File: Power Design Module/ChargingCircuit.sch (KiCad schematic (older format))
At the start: 19 parts

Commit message: Charging circuit and rough layout
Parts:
- removed C?: C_Small, symbol Device:C_Small
- added JP?: Charging Current, symbol Jumper:Jumper_3_Open
- added R?: 2K, symbol Device:R_Small_US
- added R?: 8900 R, symbol Device:R_Small_US
- D?: value LED_Small_ALT -> Green; Manfacturing # (none) -> 599-0181-007F
- D?: value LED_Small_ALT -> Red; Manfacturing # (none) -> 599-0110-007F
- JP?: value SolderJumper_2_Open -> TMR OFF
- R?: value R_Small_US -> 2K
- R?: value R_Small_US -> 200k
- R?: value R_Small_US -> 1780 R
- R?: value R_Small_US -> 49.9k
- R? (x2): value R_Small_US -> 10k
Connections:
- net EN1: now also U?.6 (EN1)
- net EN2: now also U?.5 (EN2)
- net GND: now also R?.2, U?.15 (TD), R?.2, R?.2
- net at U?.12 (ILIM): now also R?.1
- net at U?.14 (TMR): now also JP?.1 (A)
- net at U?.16 (ISET): now also JP?.2 (C); no longer R?.1
- net BATT+: now reaches J?.1 (Pin_1), JP?.1 (A), U?.2 (BAT), U?.3 (BAT)
- net ~CE: now reaches U?.4 (~CE)
- net ~CE: now also R?.1
- new net: JP?.3 (B), R?.1
- new net: JP?.1 (A), R?.1
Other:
- note added: "3 + 2 -> 100mA\n1 + 2 -> 500mA"
- note added: "Jumper Configurations"
- note added: "NOTE:\ni_lim is the maximum input current set by the following ratio:\ni_lim = k_ilim / R_ilim.\nWhere k_ilim approx 1600. \nThis design i_lim is set to 800mA see 9.4 in datasheet for details."
- moved on the sheet: D?, JP?, R?

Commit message: Changes to .gitignore file
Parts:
- added D?: Green, LED_SMD:LED_0805_2012Metric_Pad1.15x1.40mm_HandSolder, symbol Device:LED_Small_ALT
- added R?: R_Small_US, symbol Device:R_Small_US
- added SW?: Charge Disable Switch, symbol Switch:SW_DIP_x01
- D? (x2): footprint (none) -> LED_SMD:LED_0805_2012Metric_Pad1.15x1.40mm_HandSolder
- J?: footprint (none) -> Connector_USB:USB_Micro-B_Molex-105017-0001
- J?: value Conn_01x02 -> Battery Output
- JP? (x2): footprint (none) -> Connector_PinHeader_2.54mm:PinHeader_1x03_P2.54mm_Vertical
- JP?: footprint (none) -> Jumper:SolderJumper-2_P1.3mm_Open_RoundedPad1.0x1.5mm
- R?: value 1780 R -> 1.78k; footprint (none) -> Resistor_SMD:R_0805_2012Metric_Pad1.15x1.40mm_HandSolder; Manfacturing # (none) -> RC0805FR-101K78L
- R?: value 2K -> 5k
- R?: value 8900 R -> 8.98k; footprint (none) -> Resistor_SMD:R_0805_2012Metric_Pad1.15x1.40mm_HandSolder; Manfacturing # (none) -> PFC-W0805LF-03-8981-B
- R? (x2): footprint (none) -> Resistor_SMD:R_0603_1608Metric_Pad1.05x0.95mm_HandSolder
- SW?: value SW_DIP_x02 -> Input Current Selection
- U?: footprint RGT16_1P7X1P7 -> BQ24072TRGTR:BQ24072TRGTR
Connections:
- net GND: now also R?.2
- net Vbus: now also SW?.2
- net Vout: now also D?.2 (A)
- net ~CE: now also SW?.1
- new net: D?.1 (K), R?.1
- no-connect marks 1 -> 3
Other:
- note added: "- All jumpers need a 0.1" (2.54mm) jumper."
- note added: "0 0 100mA\n0 1 500mA\n1 0 Ilim\n1 1 USB Standby"
- note added: "3 + 2 -> 500mA\n1 + 2 -> 100mA"
- note added: "Battery CC charger Jumper Configurations"
- note added: "Input Current Limit"
- note added: "NOTES:\n- i_lim is the maximum input current set by the following ratio:\ni_lim = k_ilim / R_ilim.\nWhere k_ilim approx 1600. \nMaking the resistance R = 2k\nThis design i_lim is set to 800mA see 9.4 in datasheet for details."
- note added: "Switch is normaly open.\nTurn to ON to Disable Charge"
- note removed: "0 0 100mA\n0 1 500mA\n1 0 Iset\n1 1 USB Standby"
- note removed: "3 + 2 -> 100mA\n1 + 2 -> 500mA"
- note removed: "Jumper Configurations"
- note removed: "NOTE:\ni_lim is the maximum input current set by the following ratio:\ni_lim = k_ilim / R_ilim.\nWhere k_ilim approx 1600. \nThis design i_lim is set to 800mA see 9.4 in datasheet for details."
- moved on the sheet: J?, R?, SW?

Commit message: Finalized Charge board
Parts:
- removed JP?: Charging Current, Connector_PinHeader_2.54mm:PinHeader_1x03_P2.54mm_Vertical, symbol Jumper:Jumper_3_Open
- removed R?: 5k, symbol Device:R_Small_US
- removed R?: 8.98k, Resistor_SMD:R_0805_2012Metric_Pad1.15x1.40mm_HandSolder, symbol Device:R_Small_US
- added C?: 4.7uF, Capacitor_SMD:C_0805_2012Metric_Pad1.15x1.40mm_HandSolder, symbol Device:C_Small
- added R?: 2K, Resistor_SMD:R_0603_1608Metric_Pad1.05x0.95mm_HandSolder, symbol Device:R_Small_US
- C?: value C_Small -> 4.7uF; footprint (none) -> Capacitor_SMD:C_0805_2012Metric_Pad1.15x1.40mm_HandSolder; Manfacturing # (none) -> C0805C475K4RAC7210
- C?: value C_Small -> 1uF; footprint (none) -> Capacitor_SMD:C_0805_2012Metric_Pad1.15x1.40mm_HandSolder; Manfacturing # (none) -> C0805C105K4RAC7210
- D? (x2): footprint LED_SMD:LED_0805_2012Metric_Pad1.15x1.40mm_HandSolder -> LED_SMD:LED_0603_1608Metric_Pad1.05x0.95mm_HandSolder; Manfacturing # 599-0181-007F -> SMLD12EN1WT86
- D?: footprint LED_SMD:LED_0805_2012Metric_Pad1.15x1.40mm_HandSolder -> LED_SMD:LED_0603_1608Metric_Pad1.05x0.95mm_HandSolder
- J?: footprint (none) -> Connector_JST:JST_PH_S2B-PH-K_1x02_P2.00mm_Horizontal; Manfacturing # (none) -> S2B-PH-K-S(LF)(SN)
- R?: footprint (none) -> Resistor_SMD:R_0603_1608Metric_Pad1.05x0.95mm_HandSolder; Manfacturing # (none) -> RN73R1JTTD2001B25
- R?: footprint (none) -> Resistor_SMD:R_0603_1608Metric_Pad1.05x0.95mm_HandSolder; Manfacturing # (none) -> RN73R1JTTD2003B25
- R?: footprint (none) -> Resistor_SMD:R_0603_1608Metric_Pad1.05x0.95mm_HandSolder; Manfacturing # (none) -> CRCW060349K9FKEAC
- R?: value R_Small_US -> 530R; footprint (none) -> Resistor_SMD:R_0603_1608Metric_Pad1.05x0.95mm_HandSolder; Manfacturing # (none) -> RN731JTTD5300F100
- R? (x2): value R_Small_US -> 320R; footprint (none) -> Resistor_SMD:R_0603_1608Metric_Pad1.05x0.95mm_HandSolder; Manfacturing # (none) -> RT0603DRE07320RL
- R? (x2): Manfacturing # (none) -> SG73G1JTTD1002D
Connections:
- net BATT+: now also C?.1
- net GND: now also R?.1, C?.2, R?.2; no longer R?.2
- net ~CE: now also R?.1
- net at U?.16 (ISET): now also R?.1
- net at D?.1 (K): now also R?.2; no longer R?.1
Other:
- moved on the sheet: R?

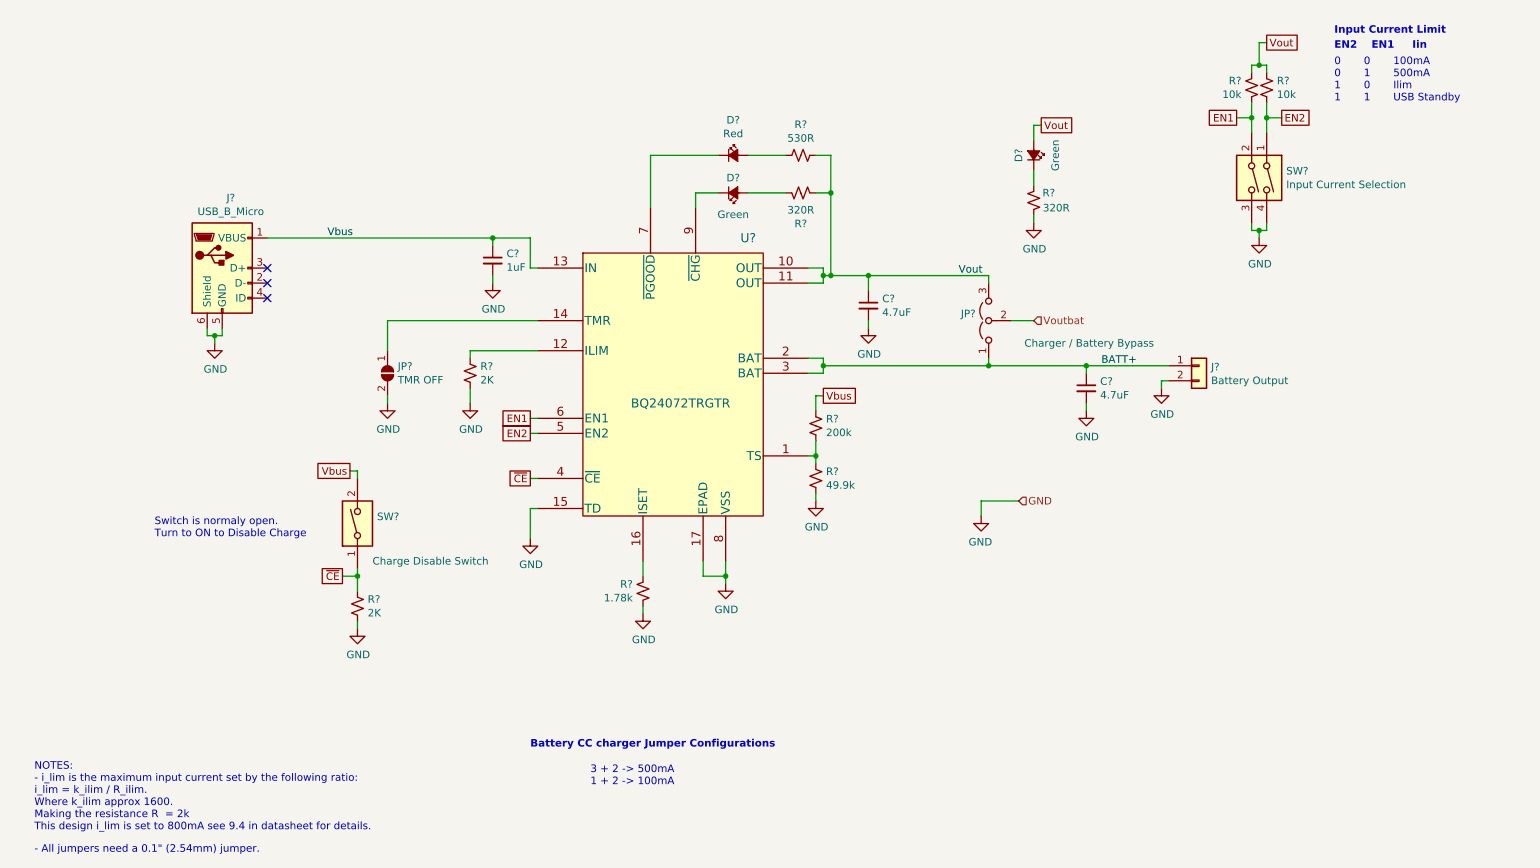
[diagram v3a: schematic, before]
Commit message: Starting Power board Layout. Design Changes
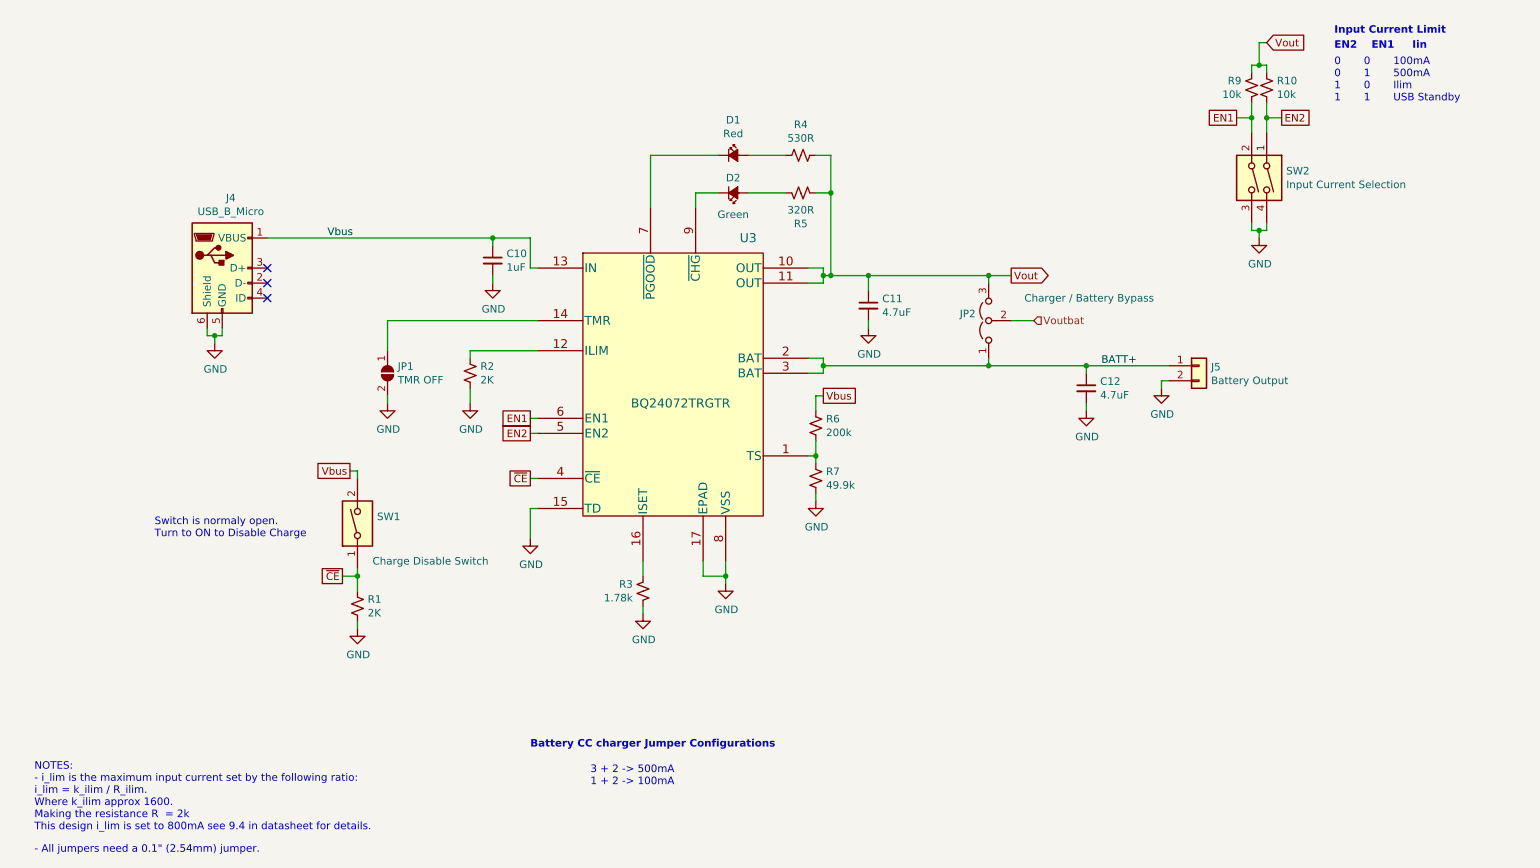
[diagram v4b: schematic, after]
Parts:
- removed D?: Green, LED_SMD:LED_0603_1608Metric_Pad1.05x0.95mm_HandSolder, symbol Device:LED_Small_ALT
- removed R?: 320R, Resistor_SMD:R_0603_1608Metric_Pad1.05x0.95mm_HandSolder, symbol Device:R_Small_US
- J4: renamed from J?; Manfacturing # (none) -> 105017-0001
- SW1: renamed from SW?; footprint (none) -> Button_Switch_SMD:SW_DIP_SPSTx01_Slide_Copal_CVS-01xB_W5.9mm_P1mm; Manfacturing # (none) -> CVS-01TB
- SW2: renamed from SW?; footprint (none) -> Button_Switch_SMD:SW_DIP_SPSTx02_Slide_Copal_CHS-02B_W7.62mm_P1.27mm; Manfacturing # (none) -> CVS-02TB
- gave numbers to parts that had none: 18
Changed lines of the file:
@@
 Text HLabel 7600 2850 2    50   Input ~ 0
 Voutbat
-Text HLabel 7500 4050 2    50   Input ~ 0
-GND
-$Comp
-L power:GND #PWR0106
-U 1 1 5E251990
-P 7250 4150
-F 0 "#PWR0106" H 7250 3900 50  0001 C CNN
-F 1 "GND" H 7255 3977 50  0000 C CNN
-F 2 "" H 7250 4150 50  0001 C CNN
-F 3 "" H 7250 4150 50  0001 C CNN
-	1    7250 4150
-	-1   0    0    -1
-$EndComp
-Wire Wire Line
-	7500 4050 7250 4050
-Wire Wire Line
-	7250 4050 7250 4150
-$Comp
-L BQ24072TRGTR:BQ24072TRGTR U?
+$Comp
+L BQ24072TRGTR:BQ24072TRGTR U3
 U 1 1 5E266BAD
 P 4600 2500
-F 0 "U?" H 5700 2700 60  0000 C CNN
+F 0 "U3" H 5700 2700 60  0000 C CNN
 F 1 "BQ24072TRGTR" H 5250 1600 60  0000 C CNN
 F 2 "BQ24072TRGTR:BQ24072TRGTR" H 5900 2900 60  0001 C CNN
@@
 $EndComp
 $Comp
-L Device:LED_Small_ALT D?
+L Device:LED_Small_ALT D2
 U 1 1 5E267CDB
 P 5600 2000
-F 0 "D?" H 5600 1900 50  0000 C CNN
+F 0 "D2" H 5600 1900 50  0000 C CNN
 F 1 "Green" H 5600 2144 50  0000 C CNN
 F 2 "LED_SMD:LED_0603_1608Metric_Pad1.05x0.95mm_HandSolder" V 5600 2000 50  0001 C CNN
@@
 $EndComp
 $Comp
-L Jumper:Jumper_3_Open JP?
+L Jumper:Jumper_3_Open JP2
 U 1 1 5E268285
 P 7300 2850
-F 0 "JP?" V 7346 2937 50  0000 L CNN
-F 1 "Charger / Battery Bypass" V 7150 1750 50  0000 L CNN
+F 0 "JP2" V 7346 2937 50  0000 L CNN
+F 1 "Charger / Battery Bypass" V 7450 1750 50  0000 L CNN
 F 2 "Connector_PinHeader_2.54mm:PinHeader_1x03_P2.54mm_Vertical" H 7300 2850 50  0001 C CNN
 F 3 "~" H 7300 2850 50  0001 C CNN
@@
 $EndComp
 $Comp
-L Jumper:SolderJumper_2_Open JP?
+L Jumper:SolderJumper_2_Open JP1
 U 1 1 5E268A70
 P 3300 3200
-F 0 "JP?" V 3254 3268 50  0000 L CNN
+F 0 "JP1" V 3254 3268 50  0000 L CNN
 F 1 "TMR OFF" V 3345 3268 50  0000 L CNN
 F 2 "Jumper:SolderJumper-2_P1.3mm_Open_RoundedPad1.0x1.5mm" H 3300 3200 50  0001 C CNN
@@
 $EndComp
 $Comp
-L Connector:USB_B_Micro J?
+L Connector:USB_B_Micro J4
 U 1 1 5E268F4D
 P 2200 2500
-F 0 "J?" H 2257 2967 50  0000 C CNN
+F 0 "J4" H 2257 2967 50  0000 C CNN
 F 1 "USB_B_Micro" H 2257 2876 50  0000 C CNN
 F 2 "Connector_USB:USB_Micro-B_Molex-105017-0001" H 2350 2450 50  0001 C CNN
 F 3 "~" H 2350 2450 50  0001 C CNN
+F 4 "105017-0001" H 2200 2500 50  0001 C CNN "Manfacturing #"
 	1    2200 2500
 	1    0    0    -1
 $EndComp
 $Comp
-L Device:C_Small C?
+L Device:C_Small C11
 U 1 1 5E26A6C2
 P 6500 2750
-F 0 "C?" H 6592 2796 50  0000 L CNN
+F 0 "C11" H 6592 2796 50  0000 L CNN
 F 1 "4.7uF" H 6592 2705 50  0000 L CNN
 F 2 "Capacitor_SMD:C_0805_2012Metric_Pad1.15x1.40mm_HandSolder" H 6500 2750 50  0001 C CNN
@@
 $EndComp
 $Comp
-L Device:R_Small_US R?
+L Device:R_Small_US R2
 U 1 1 5E26AD79
 P 3850 3200
-F 0 "R?" H 3918 3246 50  0000 L CNN
+F 0 "R2" H 3918 3246 50  0000 L CNN
 F 1 "2K" H 3918 3155 50  0000 L CNN
 F 2 "Resistor_SMD:R_0603_1608Metric_Pad1.05x0.95mm_HandSolder" H 3850 3200 50  0001 C CNN
@@
 $EndComp
 $Comp
-L Device:R_Small_US R?
+L Device:R_Small_US R6
 U 1 1 5E26B032
 P 6150 3550
-F 0 "R?" H 6218 3596 50  0000 L CNN
+F 0 "R6" H 6218 3596 50  0000 L CNN
 F 1 "200k" H 6218 3505 50  0000 L CNN
 F 2 "Resistor_SMD:R_0603_1608Metric_Pad1.05x0.95mm_HandSolder" H 6150 3550 50  0001 C CNN
@@
 $EndComp
 $Comp
-L Device:R_Small_US R?
+L Device:R_Small_US R3
 U 1 1 5E26B313
 P 5000 4650
-F 0 "R?" H 5068 4696 50  0000 L CNN
+F 0 "R3" H 5068 4696 50  0000 L CNN
 F 1 "1.78k" H 5068 4605 50  0000 L CNN
 F 2 "Resistor_SMD:R_0805_2012Metric_Pad1.15x1.40mm_HandSolder" H 5000 4650 50  0001 C CNN
@@
 $EndComp
 $Comp
-L Device:R_Small_US R?
+L Device:R_Small_US R7
 U 1 1 5E2716A5
 P 6150 3900
-F 0 "R?" H 6218 3946 50  0000 L CNN
+F 0 "R7" H 6218 3946 50  0000 L CNN
 F 1 "49.9k" H 6218 3855 50  0000 L CNN
 F 2 "Resistor_SMD:R_0603_1608Metric_Pad1.05x0.95mm_HandSolder" H 6150 3900 50  0001 C CNN
@@
 $EndComp
 $Comp
-L Device:LED_Small_ALT D?
+L Device:LED_Small_ALT D1
 U 1 1 5E273FF3
 P 5600 1750
-F 0 "D?" H 5600 1985 50  0000 C CNN
+F 0 "D1" H 5600 1985 50  0000 C CNN
 F 1 "Red" H 5600 1894 50  0000 C CNN
 F 2 "LED_SMD:LED_0603_1608Metric_Pad1.05x0.95mm_HandSolder" V 5600 1750 50  0001 C CNN
@@
 $EndComp
 $Comp
-L Device:R_Small_US R?
+L Device:R_Small_US R4
 U 1 1 5E274247
 P 6050 1750
-F 0 "R?" V 5845 1750 50  0000 C CNN
+F 0 "R4" V 5845 1750 50  0000 C CNN
 F 1 "530R" V 5936 1750 50  0000 C CNN
 F 2 "Resistor_SMD:R_0603_1608Metric_Pad1.05x0.95mm_HandSolder" H 6050 1750 50  0001 C CNN
@@
 $EndComp
 $Comp
-L Device:R_Small_US R?
+L Device:R_Small_US R5
 U 1 1 5E2748E6
 P 6050 2000
-F 0 "R?" V 5845 2000 50  0000 C CNN
+F 0 "R5" V 5845 2000 50  0000 C CNN
 F 1 "320R" V 5936 2000 50  0000 C CNN
 F 2 "Resistor_SMD:R_0603_1608Metric_Pad1.05x0.95mm_HandSolder" H 6050 2000 50  0001 C CNN
@@
 	6250 2000 6250 1750
 $Comp
-L Connector_Generic:Conn_01x02 J?
+L Connector_Generic:Conn_01x02 J5
 U 1 1 5E2791AB
 P 8700 3150
-F 0 "J?" H 8780 3142 50  0000 L CNN
+F 0 "J5" H 8780 3142 50  0000 L CNN
 F 1 "Battery Output" H 8780 3051 50  0000 L CNN
 F 2 "Connector_JST:JST_PH_S2B-PH-K_1x02_P2.00mm_Horizontal" H 8700 3150 50  0001 C CNN
@@
 Vbus
 $Comp
-L Switch:SW_DIP_x02 SW?
+L Switch:SW_DIP_x02 SW2
 U 1 1 5E2D5AAA
 P 9050 1900
-F 0 "SW?" V 9004 2130 50  0000 L CNN
+F 0 "SW2" V 9004 2130 50  0000 L CNN
 F 1 "Input Current Selection" V 9095 2130 50  0000 L CNN
-F 2 "" H 9050 1900 50  0001 C CNN
+F 2 "Button_Switch_SMD:SW_DIP_SPSTx02_Slide_Copal_CHS-02B_W7.62mm_P1.27mm" H 9050 1900 50  0001 C CNN
 F 3 "~" H 9050 1900 50  0001 C CNN
+F 4 "CVS-02TB" H 9050 1900 50  0001 C CNN "Manfacturing #"
 	1    9050 1900
 	0    1    1    0
 $EndComp
-Text GLabel 9150 1000 2    50   UnSpc ~ 0
+Text GLabel 9150 1000 2    50   Input ~ 0
 Vout
 Text GLabel 8950 1500 0    50   UnSpc ~ 0
@@
 EN2
 $Comp
-L Device:R_Small_US R?
+L Device:R_Small_US R9
 U 1 1 5E2E11CE
 P 9050 1300
-F 0 "R?" H 8982 1254 50  0000 R CNN
+F 0 "R9" H 8982 1254 50  0000 R CNN
 F 1 "10k" H 8982 1345 50  0000 R CNN
 F 2 "Resistor_SMD:R_0603_1608Metric_Pad1.05x0.95mm_HandSolder" H 9050 1300 50  0001 C CNN
@@
 $EndComp
 $Comp
-L Device:R_Small_US R?
+L Device:R_Small_US R10
 U 1 1 5E2E2CB5
 P 9150 1300
-F 0 "R?" H 9218 1346 50  0000 L CNN
+F 0 "R10" H 9218 1346 50  0000 L CNN
 F 1 "10k" H 9218 1255 50  0000 L CNN
 F 2 "Resistor_SMD:R_0603_1608Metric_Pad1.05x0.95mm_HandSolder" H 9150 1300 50  0001 C CNN
@@
 Text Label 8050 3150 0    50   ~ 0
 BATT+
-Text Label 7100 2550 0    50   ~ 0
-Vout
 $Comp
 L power:GND #PWR0115
@@
 Wire Wire Line
 	5550 4550 5550 4600
-$Comp
-L Device:LED_Small_ALT D?
-U 1 1 5E26DCA9
-P 7600 1750
-F 0 "D?" H 7600 1650 50  0000 C CNN
-F 1 "Green" H 7600 1894 50  0000 C CNN
-F 2 "LED_SMD:LED_0603_1608Metric_Pad1.05x0.95mm_HandSolder" V 7600 1750 50  0001 C CNN
-F 3 "https://www.mouser.com/datasheet/2/348/smld12-e-1510650.pdf" V 7600 1750 50  0001 C CNN
-F 4 "SMLD12EN1WT86" H 7600 1750 50  0001 C CNN "Manfacturing #"
-	1    7600 1750
-	0    1    -1   0
-$EndComp
-$Comp
-L Device:R_Small_US R?
-U 1 1 5E275A1E
-P 7600 2050
-F 0 "R?" H 7700 2000 50  0000 C CNN
-F 1 "320R" H 7750 2100 50  0000 C CNN
-F 2 "Resistor_SMD:R_0603_1608Metric_Pad1.05x0.95mm_HandSolder" H 7600 2050 50  0001 C CNN
-F 3 "~" H 7600 2050 50  0001 C CNN
-F 4 "RT0603DRE07320RL" H 7600 2050 50  0001 C CNN "Manfacturing #"
-	1    7600 2050
-	1    0    0    1
-$EndComp
-$Comp
-L power:GND #PWR0120
-U 1 1 5E2763EE
-P 7600 2200
-F 0 "#PWR0120" H 7600 1950 50  0001 C CNN
-F 1 "GND" H 7605 2027 50  0000 C CNN
-F 2 "" H 7600 2200 50  0001 C CNN
-F 3 "" H 7600 2200 50  0001 C CNN
-	1    7600 2200
-	1    0    0    -1
-$EndComp
-Wire Wire Line
-	7600 1850 7600 1950
-Wire Wire Line
-	7600 2150 7600 2200
 Text Notes 9600 950  0    50   ~ 10
 Input Current Limit
@@
 Vbus
 $Comp
-L Switch:SW_DIP_x01 SW?
+L Switch:SW_DIP_x01 SW1
 U 1 1 5E2C2193
 P 3100 4200
-F 0 "SW?" V 3146 4070 50  0000 R CNN
+F 0 "SW1" V 3146 4070 50  0000 R CNN
 F 1 "Charge Disable Switch" V 2850 4100 50  0000 R CNN
-F 2 "" H 3100 4200 50  0001 C CNN
+F 2 "Button_Switch_SMD:SW_DIP_SPSTx01_Slide_Copal_CVS-01xB_W5.9mm_P1mm" H 3100 4200 50  0001 C CNN
 F 3 "~" H 3100 4200 50  0001 C CNN
+F 4 "CVS-01TB" H 3100 4200 50  0001 C CNN "Manfacturing #"
 	1    3100 4200
 	0    -1   -1   0
@@
 Wire Wire Line
 	3100 3850 3100 3900
-Text GLabel 7650 1550 2    50   UnSpc ~ 0
-Vout
-Wire Wire Line
-	7600 1650 7600 1550
-Wire Wire Line
-	7600 1550 7650 1550
 Text Notes 1750 4300 0    50   ~ 0
 Switch is normaly open.\nTurn to ON to Disable Charge
@@
 	5000 4450 5000 4550
 $Comp
-L Device:R_Small_US R?
+L Device:R_Small_US R1
 U 1 1 5E2BBF23
 P 3100 4750
-F 0 "R?" H 3168 4796 50  0000 L CNN
+F 0 "R1" H 3168 4796 50  0000 L CNN
 F 1 "2K" H 3168 4705 50  0000 L CNN
 F 2 "Resistor_SMD:R_0603_1608Metric_Pad1.05x0.95mm_HandSolder" H 3100 4750 50  0001 C CNN
@@
 $EndComp
 $Comp
-L Device:C_Small C?
+L Device:C_Small C10
 U 1 1 5E2837DF
 P 4000 2450
-F 0 "C?" H 4092 2496 50  0000 L CNN
+F 0 "C10" H 4092 2496 50  0000 L CNN
 F 1 "1uF" H 4092 2405 50  0000 L CNN
 F 2 "Capacitor_SMD:C_0805_2012Metric_Pad1.15x1.40mm_HandSolder" H 4000 2450 50  0001 C CNN
@@
 $EndComp
 $Comp
-L Device:C_Small C?
+L Device:C_Small C12
 U 1 1 5E2D0032
 P 7950 3300
-F 0 "C?" H 8042 3346 50  0000 L CNN
+F 0 "C12" H 8042 3346 50  0000 L CNN
 F 1 "4.7uF" H 8042 3255 50  0000 L CNN
 F 2 "Capacitor_SMD:C_0805_2012Metric_Pad1.15x1.40mm_HandSolder" H 7950 3300 50  0001 C CNN
@@
 $EndComp
 $Comp
-L power:GND #PWR?
+L power:GND #PWR07
 U 1 1 5E2D0038
 P 7950 3450
-F 0 "#PWR?" H 7950 3200 50  0001 C CNN
+F 0 "#PWR07" H 7950 3200 50  0001 C CNN
 F 1 "GND" H 7955 3277 50  0000 C CNN
 F 2 "" H 7950 3450 50  0001 C CNN
@@
 Wire Wire Line
 	7950 3150 8500 3150
+Text GLabel 7450 2550 2    50   Output ~ 0
+Vout
+Wire Wire Line
+	7300 2550 7450 2550
+Connection ~ 7300 2550
 $EndSCHEMATC
